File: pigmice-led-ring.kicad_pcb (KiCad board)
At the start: 2 copper layers, 46 x 51 mm, 59 parts, among them J1 Conn_01x02_Female, J2 Conn_01x03_Female, U1 LMR62014XMF

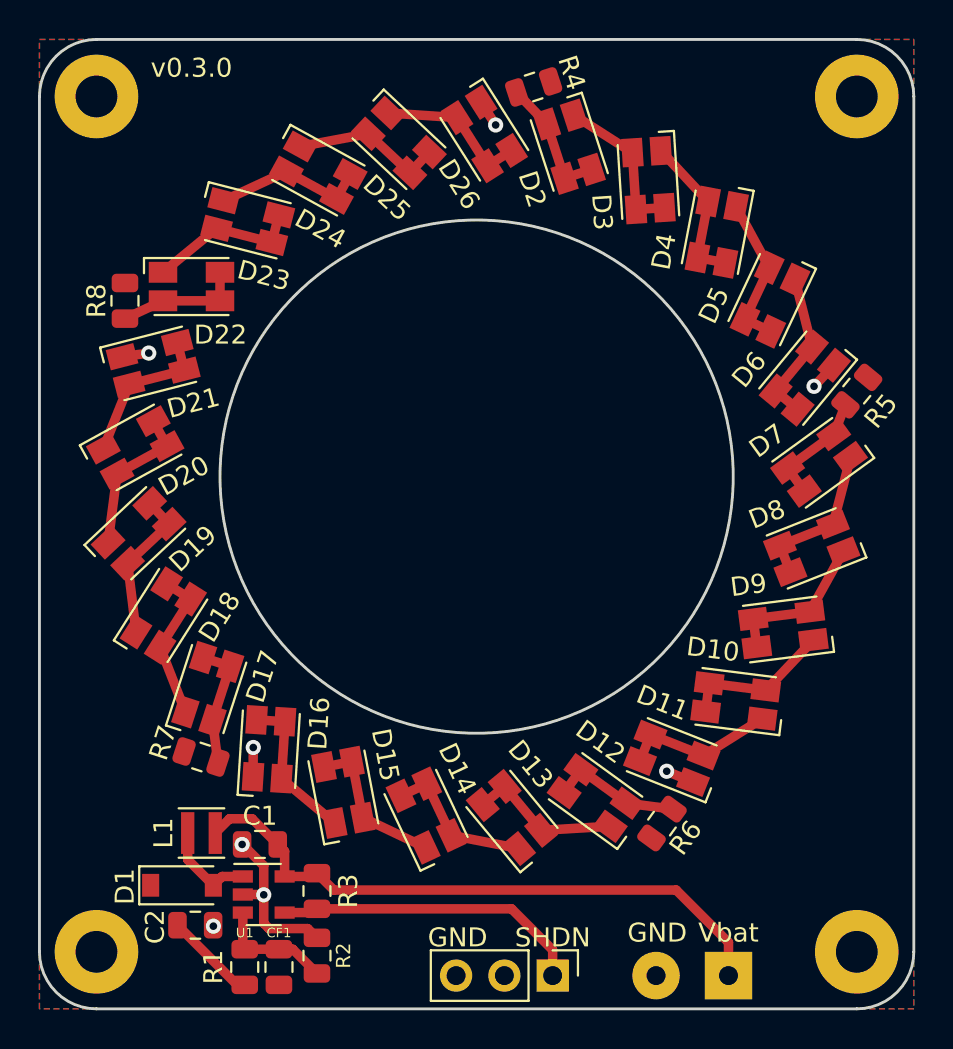
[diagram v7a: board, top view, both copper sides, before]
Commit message: Use CCRs instead of resistors
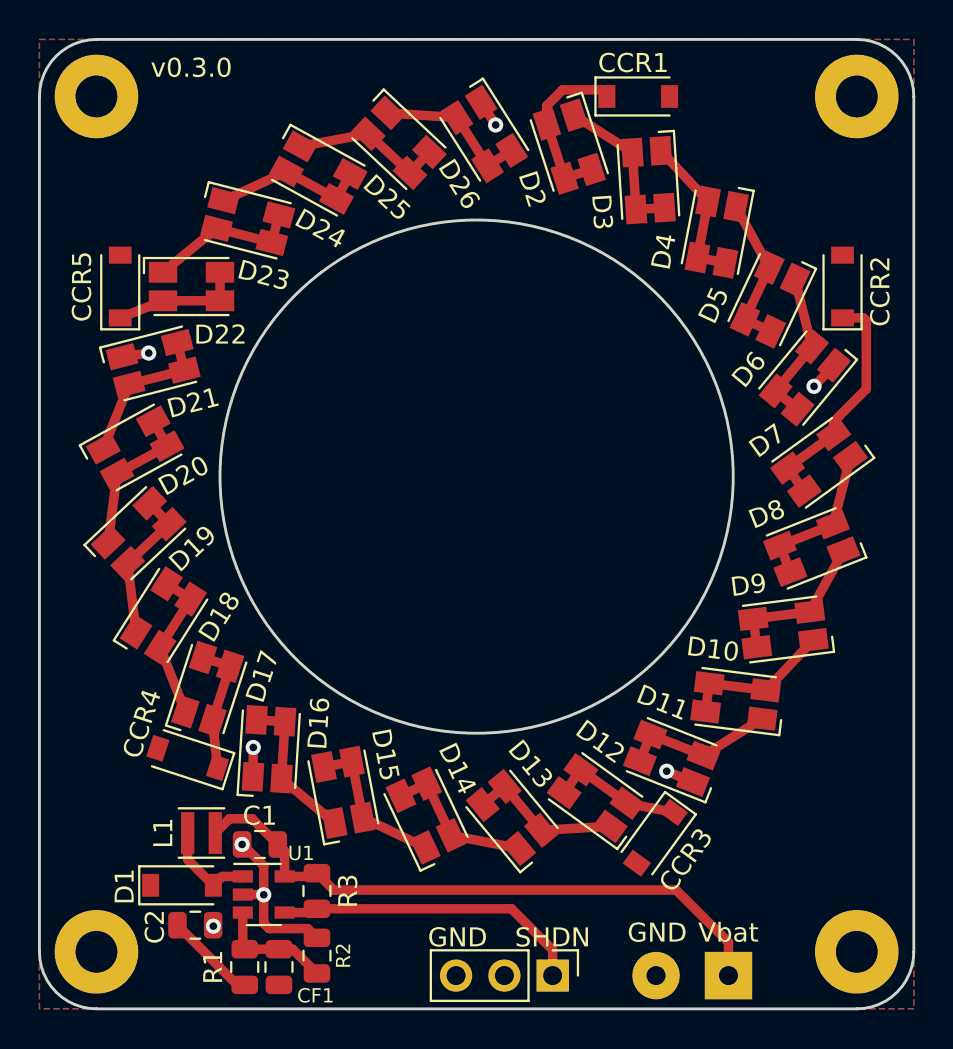
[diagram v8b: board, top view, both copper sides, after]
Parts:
- removed the G*** at (84.0, 99.5)
- removed the G*** at (107.0, 70.5)
- removed the G*** at (79.0, 60.0)
- removed the G*** at (102.0, 61.0)
- removed the G*** at (90.0, 62.0)
- removed the G*** at (108.0, 80.0)
- removed the G*** at (96.5, 99.0)
- removed the G*** at (76.5, 65.0)
- removed the G*** at (71.8, 80.0)
- removed the G*** at (107.0, 89.0)
- removed the G*** at (73.0, 89.0)
- removed the G*** at (73.0, 70.0)
- removed the G*** at (104.0, 65.0)
- removed R4, R5, R6, R7, R8: 137Ω, Resistor_SMD:R_0805_2012Metric
- added CCR1: 25mA, Diode_SMD:D_SOD-123, F.Cu at (98.5, 60.0)
- added CCR2: 25mA, Diode_SMD:D_SOD-123, F.Cu at (109.2, 70.0)
- added CCR3: 25mA, Diode_SMD:D_SOD-123, F.Cu at (99.4, 99.0)
- added CCR4: 25mA, Diode_SMD:D_SOD-123, F.Cu at (74.8, 94.8)
- added CCR5: 25mA, Diode_SMD:D_SOD-123, F.Cu at (71.2, 70.0)
- moved G*** 0.36 mm to (109.2, 96.8)
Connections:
- J2 pad 2: Net-(J2-Pad2) -> (no net)
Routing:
- net Net-(CCR2-Pad1): track 6.18 -> 12.5 mm
- net Net-(CCR1-Pad1): track 6.80 -> 9.20 mm
